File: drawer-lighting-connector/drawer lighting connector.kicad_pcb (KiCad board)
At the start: 2 copper layers, 45 x 10 mm, 2 parts, among them P1 CONN_01X04, P2 CONN_01X04

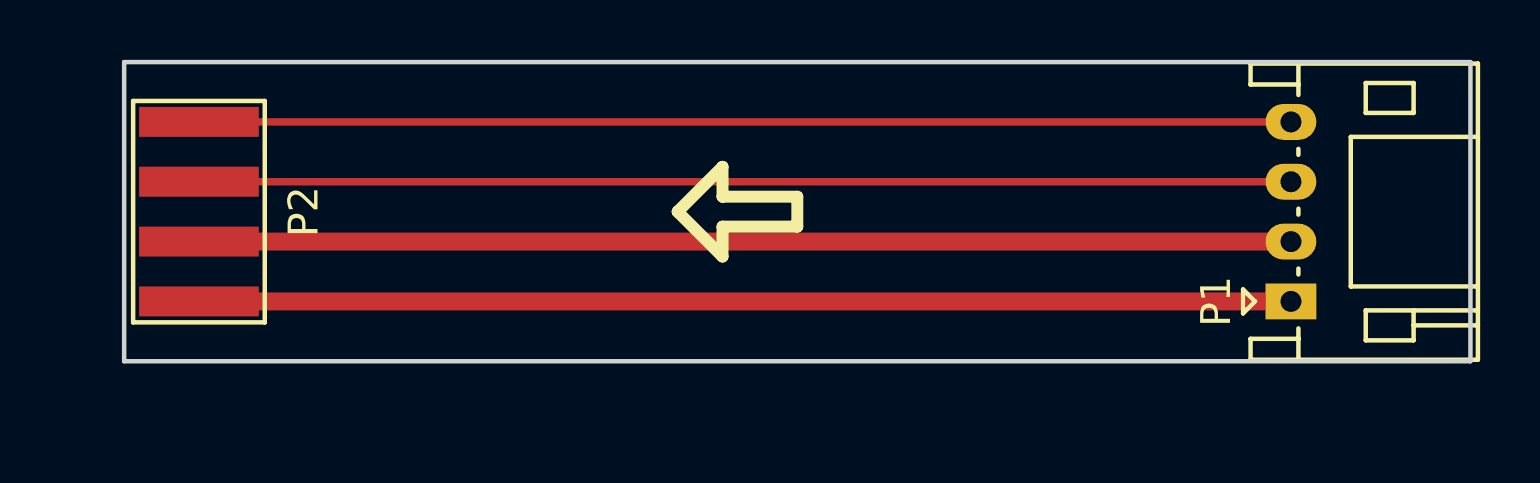
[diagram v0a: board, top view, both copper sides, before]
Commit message: Make +5V and GND traces wider and change the connector
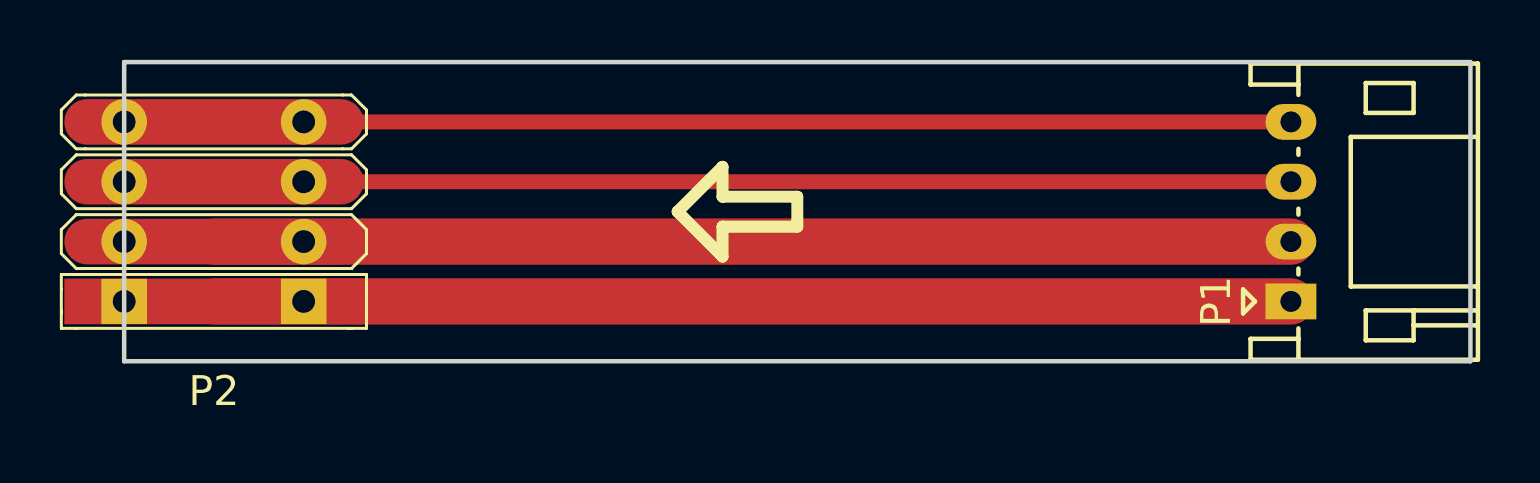
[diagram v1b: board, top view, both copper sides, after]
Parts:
- P2: footprint Pad:FourPad_2.0mm -> Pad:FourPad_2.0mm_FrontPTH_Side
- moved P2 0.50 mm to (93.0, 70.0), turned to 0 degrees
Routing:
- net GND: track 36.5 -> 36.0 mm
- net /Out: track 36.5 -> 36.0 mm
- net /In: track 36.5 -> 36.0 mm
- net +5V: track 36.5 -> 36.0 mm
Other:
- net class Default: trace_width 0.25 -> 0.5
- net class VCC: trace_width 0.6 -> 1.55
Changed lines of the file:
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@@
 (kicad_pcb (version 4) (host pcbnew 4.0.3+e1-6302~38~ubuntu15.04.1-stable)
   (general
-    (links 4)
+    (links 12)
     (no_connects 0)
-    (area 89.924999 64.324999 135.975001 78.075)
+    (area 89.924999 64.924999 135.075001 75.075001)
     (thickness 1.6)
     (drawings 11)
@@
   )
   (setup
-    (last_trace_width 0.25)
+    (last_trace_width 0.5)
     (trace_clearance 0.2)
     (zone_clearance 0.508)
@@
   (net_class Default "This is the default net class."
     (clearance 0.2)
-    (trace_width 0.25)
+    (trace_width 0.5)
     (via_dia 0.6)
     (via_drill 0.4)
@@
   (net_class VCC ""
     (clearance 0.2)
-    (trace_width 0.6)
+    (trace_width 1.55)
     (via_dia 0.6)
     (via_drill 0.4)
@@
       (net 4 /Out))
   )
-  (module Pad:FourPad_2.0mm (layer F.Cu)
-    (at 92.5 70 180)
-    (fp_text reference P2 (at -3.5 0 270) (layer F.SilkS)
-      (effects (font (size 1 1) (thickness 0.15)))
-    )
-    (fp_text value CONN_01X04 (at -2.5 -7 180) (layer F.Fab)
-      (effects (font (size 1 1) (thickness 0.15)))
-    )
-    (fp_line (start 2.2 -3.7) (end 2.2 3.7) (layer F.SilkS) (width 0.15))
-    (fp_line (start 2.2 3.7) (end -2.2 3.7) (layer F.SilkS) (width 0.15))
-    (fp_line (start -2.2 3.7) (end -2.2 -3.7) (layer F.SilkS) (width 0.15))
-    (fp_line (start -2.2 -3.7) (end 2.2 -3.7) (layer F.SilkS) (width 0.15))
-    (pad 4 smd rect (at 0 3 180) (size 4 1) (layers F.Cu F.Paste F.Mask)
-      (net 4 /Out))
-    (pad 3 smd rect (at 0 1 180) (size 4 1) (layers F.Cu F.Paste F.Mask)
-      (net 3 /In))
-    (pad 2 smd rect (at 0 -1 180) (size 4 1) (layers F.Cu F.Paste F.Mask)
-      (net 2 +5V))
-    (pad 1 smd rect (at 0 -3 180) (size 4 1) (layers F.Cu F.Paste F.Mask)
-      (net 1 GND))
+  (module Pad:FourPad_2.0mm_FrontPTH_Side (layer F.Cu)
+    (at 93 70)
+    (fp_text reference P2 (at 0 6) (layer F.SilkS)
+      (effects (font (size 1 1) (thickness 0.15)))
+    )
+    (fp_text value CONN_01X04 (at 0 -6) (layer F.Fab)
+      (effects (font (size 1 1) (thickness 0.15)))
+    )
+    (fp_line (start -4.6 2.1) (end -5.1 2.1) (layer F.SilkS) (width 0.1))
+    (fp_line (start -5.1 2.1) (end -5.1 2.6) (layer F.SilkS) (width 0.1))
+    (fp_line (start -5.1 3.4) (end -5.1 3.9) (layer F.SilkS) (width 0.1))
+    (fp_line (start -5.1 3.9) (end -4.6 3.9) (layer F.SilkS) (width 0.1))
+    (fp_line (start 5.1 3.4) (end 5.1 3.9) (layer F.SilkS) (width 0.1))
+    (fp_line (start 5.1 3.9) (end 4.6 3.9) (layer F.SilkS) (width 0.1))
+    (fp_line (start 4.6 2.1) (end 5.1 2.1) (layer F.SilkS) (width 0.1))
+    (fp_line (start 5.1 2.1) (end 5.1 2.6) (layer F.SilkS) (width 0.1))
+    (fp_line (start 4.6 2.1) (end -4.6 2.1) (layer F.SilkS) (width 0.1))
+    (fp_line (start -5.1 2.6) (end -5.1 3.3) (layer F.SilkS) (width 0.1))
+    (fp_line (start -5.1 3.3) (end -5.1 3.4) (layer F.SilkS) (width 0.1))
+    (fp_line (start -4.6 3.9) (end 4.5 3.9) (layer F.SilkS) (width 0.1))
+    (fp_line (start 4.5 3.9) (end 4.6 3.9) (layer F.SilkS) (width 0.1))
+    (fp_line (start 5.1 3.4) (end 5.1 2.6) (layer F.SilkS) (width 0.1))
+    (fp_line (start 5.1 1.3) (end 5.1 1.4) (layer F.SilkS) (width 0.1))
+    (fp_line (start 5.1 1.4) (end 4.6 1.9) (layer F.SilkS) (width 0.1))
+    (fp_line (start 4.6 1.9) (end -4.6 1.9) (layer F.SilkS) (width 0.1))
+    (fp_line (start -4.6 1.9) (end -5.1 1.4) (layer F.SilkS) (width 0.1))
+    (fp_line (start -5.1 1.4) (end -5.1 0.6) (layer F.SilkS) (width 0.1))
+    (fp_line (start -5.1 0.6) (end -4.6 0.1) (layer F.SilkS) (width 0.1))
+    (fp_line (start -4.6 0.1) (end 4.6 0.1) (layer F.SilkS) (width 0.1))
+    (fp_line (start 4.6 0.1) (end 5.1 0.6) (layer F.SilkS) (width 0.1))
+    (fp_line (start 5.1 0.6) (end 5.1 1.3) (layer F.SilkS) (width 0.1))
+    (fp_line (start 4.6 -1.9) (end -4.6 -1.9) (layer F.SilkS) (width 0.1))
+    (fp_line (start -4.6 -1.9) (end -5.1 -1.4) (layer F.SilkS) (width 0.1))
+    (fp_line (start -5.1 -1.4) (end -5.1 -0.7) (layer F.SilkS) (width 0.1))
+    (fp_line (start -5.1 -0.7) (end -5.1 -0.6) (layer F.SilkS) (width 0.1))
+    (fp_line (start -5.1 -0.6) (end -4.6 -0.1) (layer F.SilkS) (width 0.1))
+    (fp_line (start -4.6 -0.1) (end 4.6 -0.1) (layer F.SilkS) (width 0.1))
+    (fp_line (start 4.6 -0.1) (end 5.1 -0.6) (layer F.SilkS) (width 0.1))
+    (fp_line (start 5.1 -0.6) (end 5.1 -1.4) (layer F.SilkS) (width 0.1))
+    (fp_line (start 5.1 -1.4) (end 4.6 -1.9) (layer F.SilkS) (width 0.1))
+    (fp_line (start -4.3 -3.9) (end -4.6 -3.9) (layer F.SilkS) (width 0.1))
+    (fp_line (start -4.6 -3.9) (end -5.1 -3.4) (layer F.SilkS) (width 0.1))
+    (fp_line (start -5.1 -3.4) (end -5.1 -2.7) (layer F.SilkS) (width 0.1))
+    (fp_line (start -5.1 -2.7) (end -5.1 -2.6) (layer F.SilkS) (width 0.1))
+    (fp_line (start -5.1 -2.6) (end -4.6 -2.1) (layer F.SilkS) (width 0.1))
+    (fp_line (start -4.6 -2.1) (end -4.3 -2.1) (layer F.SilkS) (width 0.1))
+    (fp_line (start -4.3 -2.1) (end 4.3 -2.1) (layer F.SilkS) (width 0.1))
+    (fp_line (start 4.3 -2.1) (end 4.6 -2.1) (layer F.SilkS) (width 0.1))
+    (fp_line (start 4.6 -2.1) (end 5.1 -2.6) (layer F.SilkS) (width 0.1))
+    (fp_line (start 5.1 -2.6) (end 5.1 -3.4) (layer F.SilkS) (width 0.1))
+    (fp_line (start 5.1 -3.4) (end 4.6 -3.9) (layer F.SilkS) (width 0.1))
+    (fp_line (start 4.6 -3.9) (end 4.3 -3.9) (layer F.SilkS) (width 0.1))
+    (fp_line (start -4.3 -3.9) (end 4.3 -3.9) (layer F.SilkS) (width 0.1))
+    (pad 1 smd rect (at 0 3) (size 10 1.524) (layers F.Cu F.Paste F.Mask)
+      (net 1 GND))
+    (pad 2 smd oval (at 0 1) (size 10 1.524) (layers F.Cu F.Paste F.Mask)
+      (net 2 +5V))
+    (pad 1 thru_hole rect (at 3 3) (size 1.524 1.524) (drill 0.762) (layers *.Cu F.Mask)
+      (net 1 GND))
+    (pad 1 thru_hole rect (at -3 3) (size 1.524 1.524) (drill 0.762) (layers *.Cu F.Mask)
+      (net 1 GND))
+    (pad 2 thru_hole circle (at 3 1) (size 1.524 1.524) (drill 0.762) (layers *.Cu F.Mask)
+      (net 2 +5V))
+    (pad 2 thru_hole circle (at -3 1) (size 1.524 1.524) (drill 0.762) (layers *.Cu F.Mask)
+      (net 2 +5V))
+    (pad 3 smd oval (at 0 -1) (size 10 1.524) (layers F.Cu F.Paste F.Mask)
+      (net 3 /In))
+    (pad 3 thru_hole circle (at 3 -1) (size 1.524 1.524) (drill 0.762) (layers *.Cu F.Mask)
+      (net 3 /In))
+    (pad 3 thru_hole circle (at -3 -1) (size 1.524 1.524) (drill 0.762) (layers *.Cu F.Mask)
+      (net 3 /In))
+    (pad 4 smd oval (at 0 -3) (size 10 1.524) (layers F.Cu F.Paste F.Mask)
+      (net 4 /Out))
+    (pad 4 thru_hole circle (at 3 -3) (size 1.524 1.524) (drill 0.762) (layers *.Cu F.Mask)
+      (net 4 /Out))
+    (pad 4 thru_hole circle (at -3 -3) (size 1.524 1.524) (drill 0.762) (layers *.Cu F.Mask)
+      (net 4 /Out))
   )
   (gr_line (start 110 69.5) (end 112.5 69.5) (angle 90) (layer F.SilkS) (width 0.4))
@@
   (gr_line (start 90 75) (end 135 75) (angle 90) (layer Edge.Cuts) (width 0.15))
   (gr_line (start 90 65) (end 90 75) (angle 90) (layer Edge.Cuts) (width 0.15))
-  (segment (start 129 73) (end 92.5 73) (width 0.6) (layer F.Cu) (net 1) (status C00000))
-  (segment (start 92.5 71) (end 129 71) (width 0.6) (layer F.Cu) (net 2) (status C00000))
-  (segment (start 129 69) (end 92.5 69) (width 0.25) (layer F.Cu) (net 3) (status C00000))
-  (segment (start 92.5 67) (end 129 67) (width 0.25) (layer F.Cu) (net 4) (status C00000))
+  (segment (start 93 73) (end 129 73) (width 1.55) (layer F.Cu) (net 1))
+  (segment (start 93 71) (end 129 71) (width 1.55) (layer F.Cu) (net 2))
+  (segment (start 129 69) (end 93 69) (width 0.5) (layer F.Cu) (net 3))
+  (segment (start 93 67) (end 129 67) (width 0.5) (layer F.Cu) (net 4))
 )

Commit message: Add more traces
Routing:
- net GND: track 36.0 -> 75.0 mm
- net /Out: track 36.0 -> 75.0 mm
- net /In: track 36.0 -> 75.0 mm
- net +5V: track 36.0 -> 75.0 mm
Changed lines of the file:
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@@
     (links 12)
     (no_connects 0)
-    (area 89.924999 64.924999 135.075001 75.075001)
+    (area 87.649999 63.025 135.975001 78.075)
     (thickness 1.6)
     (drawings 11)
-    (tracks 4)
+    (tracks 12)
     (zones 0)
     (modules 2)
@@
   (gr_line (start 90 75) (end 135 75) (angle 90) (layer Edge.Cuts) (width 0.15))
   (gr_line (start 90 65) (end 90 75) (angle 90) (layer Edge.Cuts) (width 0.15))
-  (segment (start 93 73) (end 129 73) (width 1.55) (layer F.Cu) (net 1))
-  (segment (start 93 71) (end 129 71) (width 1.55) (layer F.Cu) (net 2))
-  (segment (start 129 69) (end 93 69) (width 0.5) (layer F.Cu) (net 3))
-  (segment (start 93 67) (end 129 67) (width 0.5) (layer F.Cu) (net 4))
+  (segment (start 96 73) (end 90 73) (width 1.55) (layer B.Cu) (net 1) (status C00000))
+  (segment (start 129 73) (end 96 73) (width 1.55) (layer B.Cu) (net 1) (status C00000))
+  (segment (start 93 73) (end 129 73) (width 1.55) (layer F.Cu) (net 1) (status C00000))
+  (segment (start 96 71) (end 90 71) (width 1.55) (layer B.Cu) (net 2) (status C00000))
+  (segment (start 129 71) (end 96 71) (width 1.55) (layer B.Cu) (net 2) (status C00000))
+  (segment (start 129 71) (end 93 71) (width 1.55) (layer F.Cu) (net 2) (status C00000))
+  (segment (start 96 69) (end 90 69) (width 0.5) (layer B.Cu) (net 3) (status C00000))
+  (segment (start 129 69) (end 96 69) (width 0.5) (layer B.Cu) (net 3) (status C00000))
+  (segment (start 129 69) (end 93 69) (width 0.5) (layer F.Cu) (net 3) (status C00000))
+  (segment (start 96 67) (end 90 67) (width 0.5) (layer B.Cu) (net 4) (status C00000))
+  (segment (start 129 67) (end 96 67) (width 0.5) (layer B.Cu) (net 4) (status C00000))
+  (segment (start 93 67) (end 129 67) (width 0.5) (layer F.Cu) (net 4) (status C00000))
 )
